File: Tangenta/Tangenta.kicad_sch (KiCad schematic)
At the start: 9 parts

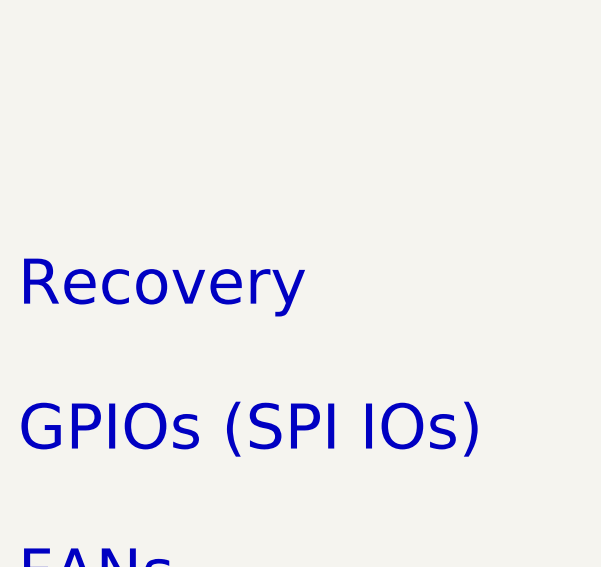
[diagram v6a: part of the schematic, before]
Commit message: Adding recovery mode jumper.
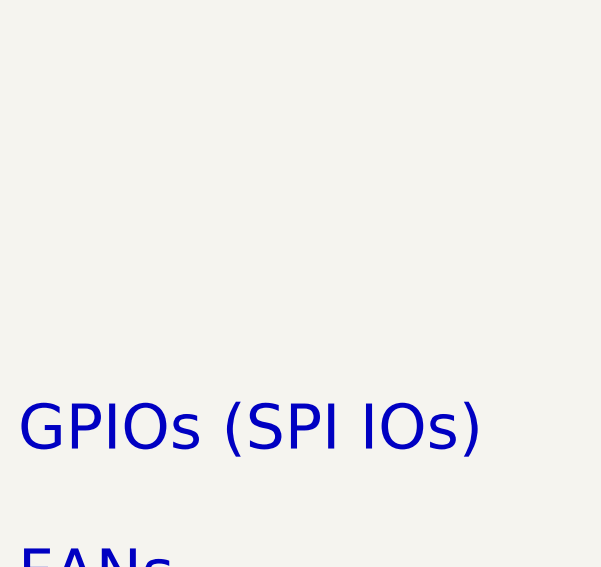
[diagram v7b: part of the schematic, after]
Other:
- note added: "GPIOs (SPI IOs) FANs ADC"
- note removed: "Recovery GPIOs (SPI IOs) FANs ADC"
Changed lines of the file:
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@@
     (stroke (width 0) (type default))
   )
-  (text "Recovery\n\nGPIOs (SPI IOs)\n\nFANs\n\nADC" (at -100.965 160.655 0)
+  (text "GPIOs (SPI IOs)\n\nFANs\n\nADC" (at -100.965 160.655 0)
     (effects (font (size 5 5)) (justify left bottom))
   )

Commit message: Adding FANs.
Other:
- added sheet FANs (FANs.kicad_sch)
- sheet Toradex ports: added 5V, PWM{1 2}; removed none
- note added: "GPIOs (SPI, IOs, ADC)"
- note removed: "GPIOs (SPI IOs) FANs ADC"
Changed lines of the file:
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@@
+    (stroke (width 0) (type default))
+  )
+  (wire (pts (xy 107.315 27.305) (xy 93.98 27.305))
+    (stroke (width 0) (type default))
+  )
+  (wire (pts (xy 277.495 273.685) (xy 279.4 273.685))
     (stroke (width 0) (type default))
   )
@@
     (stroke (width 0) (type default))
   )
-  (wire (pts (xy 277.495 273.685) (xy 279.4 273.685))
-    (stroke (width 0) (type default))
-  )
   (wire (pts (xy 327.025 52.07) (xy 340.36 52.07))
     (stroke (width 0) (type default))
@@
     (stroke (width 0) (type default))
   )
+  (wire (pts (xy 85.09 201.93) (xy 98.425 201.93))
+    (stroke (width 0) (type default))
+  )
   (wire (pts (xy 46.355 163.83) (xy 52.705 163.83))
     (stroke (width 0) (type default))
@@
     (stroke (width 0) (type default))
   )
+  (wire (pts (xy 85.09 199.39) (xy 98.425 199.39))
+    (stroke (width 0) (type default))
+  )
   (wire (pts (xy 85.09 64.77) (xy 98.425 64.77))
     (stroke (width 0) (type default))
@@
     (stroke (width 0) (type default))
   )
+  (wire (pts (xy 85.09 204.47) (xy 98.425 204.47))
+    (stroke (width 0) (type default))
+  )
   (bus (pts (xy 254.635 150.495) (xy 278.765 150.495))
     (stroke (width 0) (type default))
@@
     (stroke (width 0) (type default))
   )
+  (bus (pts (xy 85.09 210.185) (xy 107.315 210.185))
+    (stroke (width 0) (type default))
+  )
   (bus (pts (xy 188.595 161.29) (xy 294.64 161.29))
     (stroke (width 0) (type default))
@@
     (stroke (width 0) (type default))
   )
-  (text "GPIOs (SPI IOs)\n\nFANs\n\nADC" (at -100.965 160.655 0)
+  (text "GPIOs (SPI, IOs, ADC)\n" (at -100.965 160.655 0)
     (effects (font (size 5 5)) (justify left bottom))
   )
@@
     (effects (font (size 1.27 1.27)) (justify right bottom))
   )
+  (label "GND" (at 98.425 204.47 180) (fields_autoplaced)
+    (effects (font (size 1.27 1.27)) (justify right bottom))
+  )
   (label "GND" (at 98.425 72.39 180) (fields_autoplaced)
     (effects (font (size 1.27 1.27)) (justify right bottom))
@@
     (effects (font (size 1.27 1.27)) (justify left bottom))
   )
+  (label "1V8" (at 98.425 199.39 180) (fields_autoplaced)
+    (effects (font (size 1.27 1.27)) (justify right bottom))
+  )
+  (label "5V" (at 98.425 201.93 180) (fields_autoplaced)
+    (effects (font (size 1.27 1.27)) (justify right bottom))
+  )
   (label "12V" (at 402.59 24.13 180) (fields_autoplaced)
     (effects (font (size 1.27 1.27)) (justify right bottom))
@@
     (effects (font (size 1.27 1.27)) (justify right bottom))
   )
+  (label "5V" (at 93.98 24.765 0) (fields_autoplaced)
+    (effects (font (size 1.27 1.27)) (justify left bottom))
+  )
   (label "GND" (at 402.59 52.07 180) (fields_autoplaced)
     (effects (font (size 1.27 1.27)) (justify right bottom))
@@
     (effects (font (size 1.27 1.27)) (justify right bottom))
   )
-  (label "GND" (at 93.98 24.765 0) (fields_autoplaced)
+  (label "GND" (at 93.98 27.305 0) (fields_autoplaced)
     (effects (font (size 1.27 1.27)) (justify left bottom))
   )
@@
     )
   )
+  (sheet (at 52.705 196.215) (size 32.385 20.32) (fields_autoplaced)
+    (stroke (width 0.1524) (type solid))
+    (fill (color 0 0 0 0.0000))
+    (property "Sheetname" "FANs" (at 52.705 195.5034 0)
+      (effects (font (size 1.27 1.27)) (justify left bottom))
+    )
+    (property "Sheetfile" "FANs.kicad_sch" (at 52.705 217.1196 0)
+      (effects (font (size 1.27 1.27)) (justify left top) hide)
+    )
+    (pin "GND" bidirectional (at 85.09 204.47 0)
+      (effects (font (size 1.27 1.27)) (justify right))
+    )
+    (pin "5V" input (at 85.09 201.93 0)
+      (effects (font (size 1.27 1.27)) (justify right))
+    )
+    (pin "1V8" input (at 85.09 199.39 0)
+      (effects (font (size 1.27 1.27)) (justify right))
+    )
+    (pin "PWM{1 2}" input (at 85.09 210.185 0)
+      (effects (font (size 1.27 1.27)) (justify right))
+    )
+    (instances
+      (project "Tangenta"
+        (path "/358d1bcf-7599-4352-8c4d-baa18a5f09e6" (page "31"))
+      )
+    )
+  )
   (sheet (at 214.63 182.245) (size 59.69 24.765) (fields_autoplaced)
     (stroke (width 0.1524) (type solid))
@@
       (effects (font (size 1.27 1.27)) (justify right))
     )
-    (pin "GND" bidirectional (at 107.315 24.765 180)
+    (pin "GND" bidirectional (at 107.315 27.305 180)
       (effects (font (size 1.27 1.27)) (justify left))
     )
@@
       (effects (font (size 1.27 1.27)) (justify left))
     )
+    (pin "PWM{1 2}" output (at 107.315 210.185 180)
+      (effects (font (size 1.27 1.27)) (justify left))
+    )
+    (pin "5V" input (at 107.315 24.765 180)
+      (effects (font (size 1.27 1.27)) (justify left))
+    )
